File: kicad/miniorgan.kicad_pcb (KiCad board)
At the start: 2 copper layers, 202 x 125 mm, 236 parts, among them J1 Conn_01x03, J10 Conn_01x03, J11 Conn_01x03, J2 POWER_IN, J3 AudioJack3, J4 Conn_01x05, J5 Conn_01x04, J6 Conn_01x06, J7 Barrel_Jack_Switch, U1 40106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

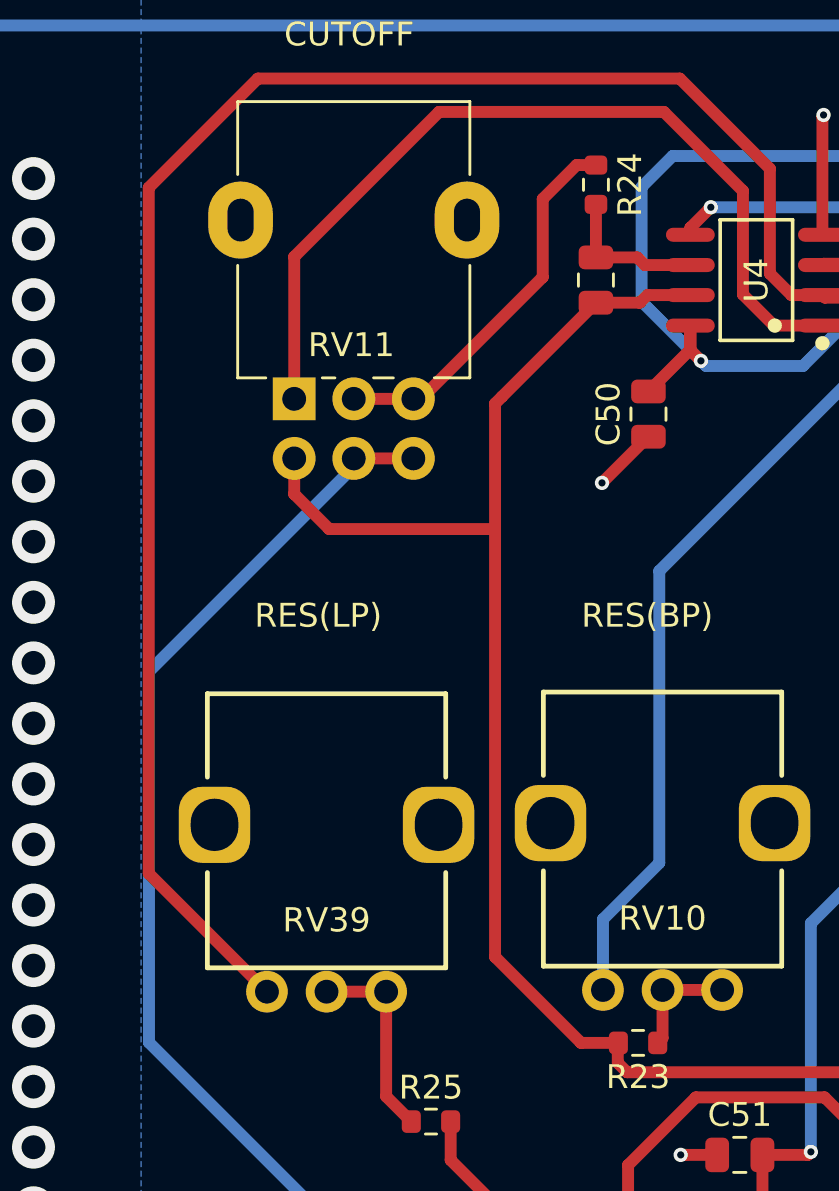
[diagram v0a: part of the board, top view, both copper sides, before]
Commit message: update footprint of dual gang potentiometer to accomodate larger poti
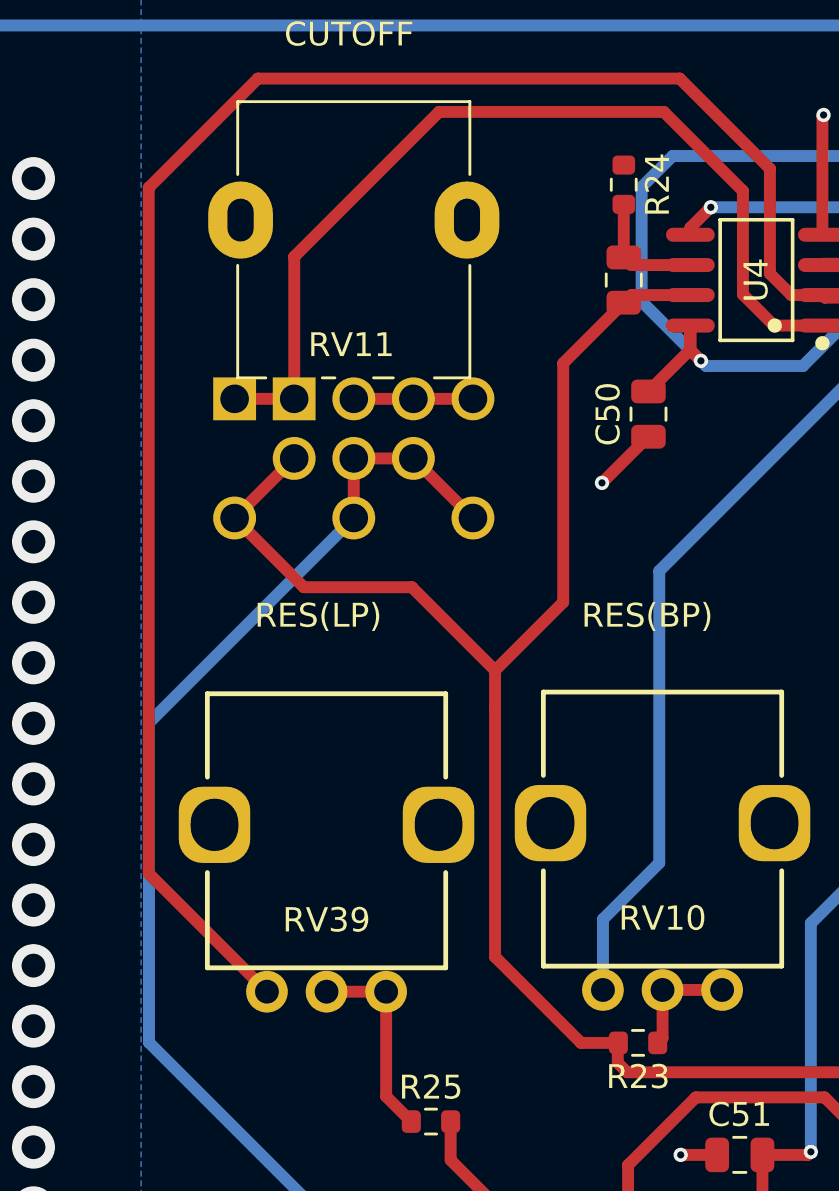
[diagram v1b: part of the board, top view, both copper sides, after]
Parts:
- moved C11 1.17 mm to (145.2, 43.1)
- moved R24 1.17 mm to (145.2, 39.1)
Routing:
- net Net-(R24-Pad1): track 16.1 -> 5.00 mm
- net /Filter/band pass: track 76.7 -> 82.6 mm
- net Net-(R26-Pad1): track 45.8 -> 49.7 mm
- net /Filter/high pass: track 68.1 -> 70.6 mm
- net Net-(U4B--): track 6.32 -> 5.15 mm
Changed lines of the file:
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@@
 	(footprint "Capacitor_SMD:C_0805_2012Metric"
 		(layer "F.Cu")
-		(at 144.0826 43.05415 -90)
+		(at 145.25 43.05415 -90)
 		(descr "Capacitor SMD 0805 (2012 Metric), square (rectangular) end terminal, IPC_7351 nominal, (Body size source: IPC-SM-782 page 76, https://www.pcb-3d.com/wordpress/wp-content/uploads/ipc-sm-782a_amendment_1_and_2.pdf, https://docs.google.com/spreadsheets/d/1BsfQQcO9C6DZCsRaXUlFlo91Tg2WpOkGARC1WS5S8t0/edit?usp=sharing), generated with kicad-footprint-generator")
 		(tags "capacitor")
@@
 	(footprint "Resistor_SMD:R_0603_1608Metric"
 		(layer "F.Cu")
-		(at 144.0826 39.05415 -90)
+		(at 145.25 39.05415 -90)
 		(descr "Resistor SMD 0603 (1608 Metric), square (rectangular) end terminal, IPC_7351 nominal, (Body size source: IPC-SM-782 page 72, https://www.pcb-3d.com/wordpress/wp-content/uploads/ipc-sm-782a_amendment_1_and_2.pdf), generated with kicad-footprint-generator")
 		(tags "resistor")
@@
 			)
 		)
+		(property "Notes" "Alternative RV16A01F-41-15R1-B1M"
+			(at 0 0 0)
+			(unlocked yes)
+			(layer "F.Fab")
+			(hide yes)
+			(effects
+				(font
+					(size 1 1)
+					(thickness 0.15)
+				)
+			)
+		)
 		(property ki_fp_filters "Potentiometer*")
 		(sheetname "Filter")
@@
 		)
 		(pad "1" thru_hole rect
+			(at 0 -2.5 180)
+			(size 1.8 1.8)
+			(drill 1.2)
+			(layers "*.Cu" "*.Mask")
+			(remove_unused_layers no)
+			(net 105 "/Filter/high pass")
+			(pinfunction "1")
+			(pintype "passive")
+		)
+		(pad "1" thru_hole rect
 			(at 0 0 180)
 			(size 1.8 1.8)
-			(drill 1)
+			(drill 1.2)
 			(layers "*.Cu" "*.Mask")
 			(remove_unused_layers no)
@@
 			(at 0 2.5 180)
 			(size 1.8 1.8)
-			(drill 1)
+			(drill 1.2)
 			(layers "*.Cu" "*.Mask")
 			(remove_unused_layers no)
@@
 			(at 0 5 180)
 			(size 1.8 1.8)
-			(drill 1)
+			(drill 1.2)
+			(layers "*.Cu" "*.Mask")
+			(remove_unused_layers no)
+			(net 106 "Net-(R24-Pad1)")
+			(pinfunction "3")
+			(pintype "passive")
+		)
+		(pad "3" thru_hole circle
+			(at 0 7.5 180)
+			(size 1.8 1.8)
+			(drill 1.2)
 			(layers "*.Cu" "*.Mask")
 			(remove_unused_layers no)
@@
 		)
 		(pad "4" thru_hole circle
+			(at -5 -2.5 180)
+			(size 1.8 1.8)
+			(drill 1.2)
+			(layers "*.Cu" "*.Mask")
+			(remove_unused_layers no)
+			(net 20 "/Filter/band pass")
+			(pinfunction "4")
+			(pintype "passive")
+		)
+		(pad "4" thru_hole circle
 			(at -2.5 0 180)
 			(size 1.8 1.8)
-			(drill 1)
+			(drill 1.2)
 			(layers "*.Cu" "*.Mask")
 			(remove_unused_layers no)
@@
 		)
 		(pad "5" thru_hole circle
+			(at -5 2.5 180)
+			(size 1.8 1.8)
+			(drill 1.2)
+			(layers "*.Cu" "*.Mask")
+			(remove_unused_layers no)
+			(net 107 "Net-(R26-Pad1)")
+			(pinfunction "5")
+			(pintype "passive")
+		)
+		(pad "5" thru_hole circle
 			(at -2.5 2.5 180)
 			(size 1.8 1.8)
-			(drill 1)
+			(drill 1.2)
 			(layers "*.Cu" "*.Mask")
 			(remove_unused_layers no)
@@
 		)
 		(pad "6" thru_hole circle
+			(at -5 7.5 180)
+			(size 1.8 1.8)
+			(drill 1.2)
+			(layers "*.Cu" "*.Mask")
+			(remove_unused_layers no)
+			(net 107 "Net-(R26-Pad1)")
+			(pinfunction "6")
+			(pintype "passive")
+		)
+		(pad "6" thru_hole circle
 			(at -2.5 5 180)
 			(size 1.8 1.8)
-			(drill 1)
+			(drill 1.2)
 			(layers "*.Cu" "*.Mask")
 			(remove_unused_layers no)
@@
 	)
 	(segment
-		(start 131.4226 52.0326)
-		(end 132.89 53.5)
+		(start 128.9226 53.03715)
+		(end 131.4226 50.53715)
 		(width 0.5)
 		(layer "F.Cu")
@@
 	)
 	(segment
-		(start 145 75.08255)
-		(end 145 75.9)
+		(start 139.85 71.44955)
+		(end 139.85 61.02)
 		(width 0.5)
 		(layer "F.Cu")
@@
 	)
 	(segment
-		(start 132.89 53.5)
-		(end 139.81 53.5)
+		(start 142.71 46.54415)
+		(end 145.25 44.00415)
+		(width 0.5)
+		(layer "F.Cu")
+		(net 20)
+	)
+	(segment
+		(start 145 75.08255)
+		(end 145 75.9)
 		(width 0.5)
 		(layer "F.Cu")
@@
 	)
 	(segment
-		(start 139.81 53.5)
-		(end 139.85 53.46)
+		(start 139.85 61.02)
+		(end 139.85 59.43)
 		(width 0.5)
 		(layer "F.Cu")
@@
 	)
 	(segment
-		(start 131.4226 50.53715)
-		(end 131.4226 52.0326)
+		(start 145.0244 75.05815)
+		(end 143.4586 75.05815)
 		(width 0.5)
 		(layer "F.Cu")
@@
 	)
 	(segment
-		(start 140.1456 47.94115)
-		(end 144.0826 44.00415)
+		(start 142.71 56.57)
+		(end 142.71 46.54415)
 		(width 0.5)
 		(layer "F.Cu")
@@
 	)
 	(segment
-		(start 139.85 71.44955)
-		(end 139.85 48.23675)
+		(start 145 75.9)
+		(end 145.39 76.29)
 		(width 0.5)
 		(layer "F.Cu")
@@
 	)
 	(segment
-		(start 145.92585 44.00415)
-		(end 146.24585 43.68415)
+		(start 148.0436 43.68415)
+		(end 145.57 43.68415)
 		(width 0.5)
 		(layer "F.Cu")
@@
 	)
 	(segment
-		(start 145 75.9)
-		(end 145.39 76.29)
+		(start 145.57 43.68415)
+		(end 145.25 44.00415)
 		(width 0.5)
 		(layer "F.Cu")
@@
 	)
 	(segment
-		(start 145.0244 75.05815)
-		(end 143.4586 75.05815)
+		(start 139.85 59.43)
+		(end 136.36 55.94)
 		(width 0.5)
 		(layer "F.Cu")
@@
 	)
 	(segment
-		(start 146.24585 43.68415)
-		(end 148.0436 43.68415)
+		(start 131.82545 55.94)
+		(end 128.9226 53.03715)
 		(width 0.5)
 		(layer "F.Cu")
@@
 	)
 	(segment
-		(start 139.85 48.23675)
-		(end 140.1456 47.94115)
+		(start 139.85 59.43)
+		(end 142.71 56.57)
 		(width 0.5)
 		(layer "F.Cu")
@@
 	)
 	(segment
-		(start 144.0826 44.00415)
-		(end 145.92585 44.00415)
+		(start 145.0244 75.05815)
+		(end 145 75.08255)
 		(width 0.5)
 		(layer "F.Cu")
@@
 	)
 	(segment
-		(start 145.0244 75.05815)
-		(end 145 75.08255)
+		(start 136.36 55.94)
+		(end 131.82545 55.94)
 		(width 0.5)
 		(layer "F.Cu")
@@
 	)
 	(segment
-		(start 144.0826 39.87915)
-		(end 144.0826 42.10415)
-		(width 0.5)
-		(layer "F.Cu")
-		(net 23)
-	)
-	(segment
-		(start 145.81415 42.10415)
-		(end 146.13415 42.42415)
+		(start 148.0436 42.42415)
+		(end 145.57 42.42415)
 		(width 0.5)
 		(layer "F.Cu")
@@
 	)
 	(segment
-		(start 144.0826 42.10415)
-		(end 145.81415 42.10415)
+		(start 145.57 42.42415)
+		(end 145.25 42.10415)
 		(width 0.5)
 		(layer "F.Cu")
@@
 	)
 	(segment
-		(start 146.13415 42.42415)
-		(end 148.0436 42.42415)
+		(start 145.25 39.87915)
+		(end 145.25 42.10415)
 		(width 0.5)
 		(layer "F.Cu")
@@
 	)
 	(segment
+		(start 128.9226 48.03715)
+		(end 131.4226 48.03715)
+		(width 0.5)
+		(layer "F.Cu")
+		(net 105)
+	)
+	(segment
 		(start 131.4226 48.03715)
 		(end 131.4226 42.0774)
@@
 	)
 	(segment
-		(start 136.74285 48.03715)
+		(start 133.9226 48.03715)
 		(end 136.4226 48.03715)
 		(width 0.5)
@@
 	)
 	(segment
-		(start 141.85 42.93)
-		(end 136.74285 48.03715)
-		(width 0.5)
-		(layer "F.Cu")
-		(net 106)
-	)
-	(segment
-		(start 141.85 39.65)
-		(end 141.85 42.93)
-		(width 0.5)
-		(layer "F.Cu")
-		(net 106)
-	)
-	(segment
-		(start 133.9226 48.03715)
-		(end 136.4226 48.03715)
+		(start 136.4226 48.03715)
+		(end 138.9226 48.03715)
 		(width 0.5)
 		(layer "F.Cu")
@@
 	)
 	(segment
-		(start 144.0826 38.22915)
-		(end 143.27085 38.22915)
+		(start 133.9226 50.53715)
+		(end 136.4226 50.53715)
 		(width 0.5)
 		(layer "F.Cu")
-		(net 106)
+		(net 107)
 	)
 	(segment
-		(start 143.27085 38.22915)
-		(end 141.85 39.65)
+		(start 136.5896 84.71015)
+		(end 135.00015 84.71015)
 		(width 0.5)
 		(layer "F.Cu")
-		(net 106)
+		(net 107)
 	)
 	(segment
 		(start 133.9226 50.53715)
-		(end 136.4226 50.53715)
+		(end 133.9226 53.03715)
 		(width 0.5)
 		(layer "F.Cu")
@@
 	)
 	(segment
-		(start 136.5896 84.71015)
-		(end 135.00015 84.71015)
+		(start 135.00015 84.71015)
+		(end 133.39 83.1)
 		(width 0.5)
 		(layer "F.Cu")
@@
 	)
 	(segment
-		(start 135.00015 84.71015)
-		(end 133.39 83.1)
+		(start 136.4226 50.53715)
+		(end 138.9226 53.03715)
 		(width 0.5)
 		(layer "F.Cu")
@@
 	)
 	(segment
-		(start 133.39 83.1)
-		(end 125.33 75.04)
+		(start 125.33 75.04)
+		(end 125.33 61.62975)
 		(width 0.5)
 		(layer "B.Cu")
@@
 	)
 	(segment
-		(start 125.33 59.48)
-		(end 133.9226 50.8874)
+		(start 133.39 83.1)
+		(end 125.33 75.04)
 		(width 0.5)
 		(layer "B.Cu")
@@
 	)
 	(segment
-		(start 133.9226 50.8874)
-		(end 133.9226 50.53715)
+		(start 125.33 61.62975)
+		(end 133.9226 53.03715)
 		(width 0.5)
 		(layer "B.Cu")
@@
 	)
 	(segment
-		(start 125.33 75.04)
-		(end 125.33 59.48)
+		(start 133.9226 50.8874)
+		(end 133.9226 50.53715)
 		(width 0.5)
 		(layer "B.Cu")

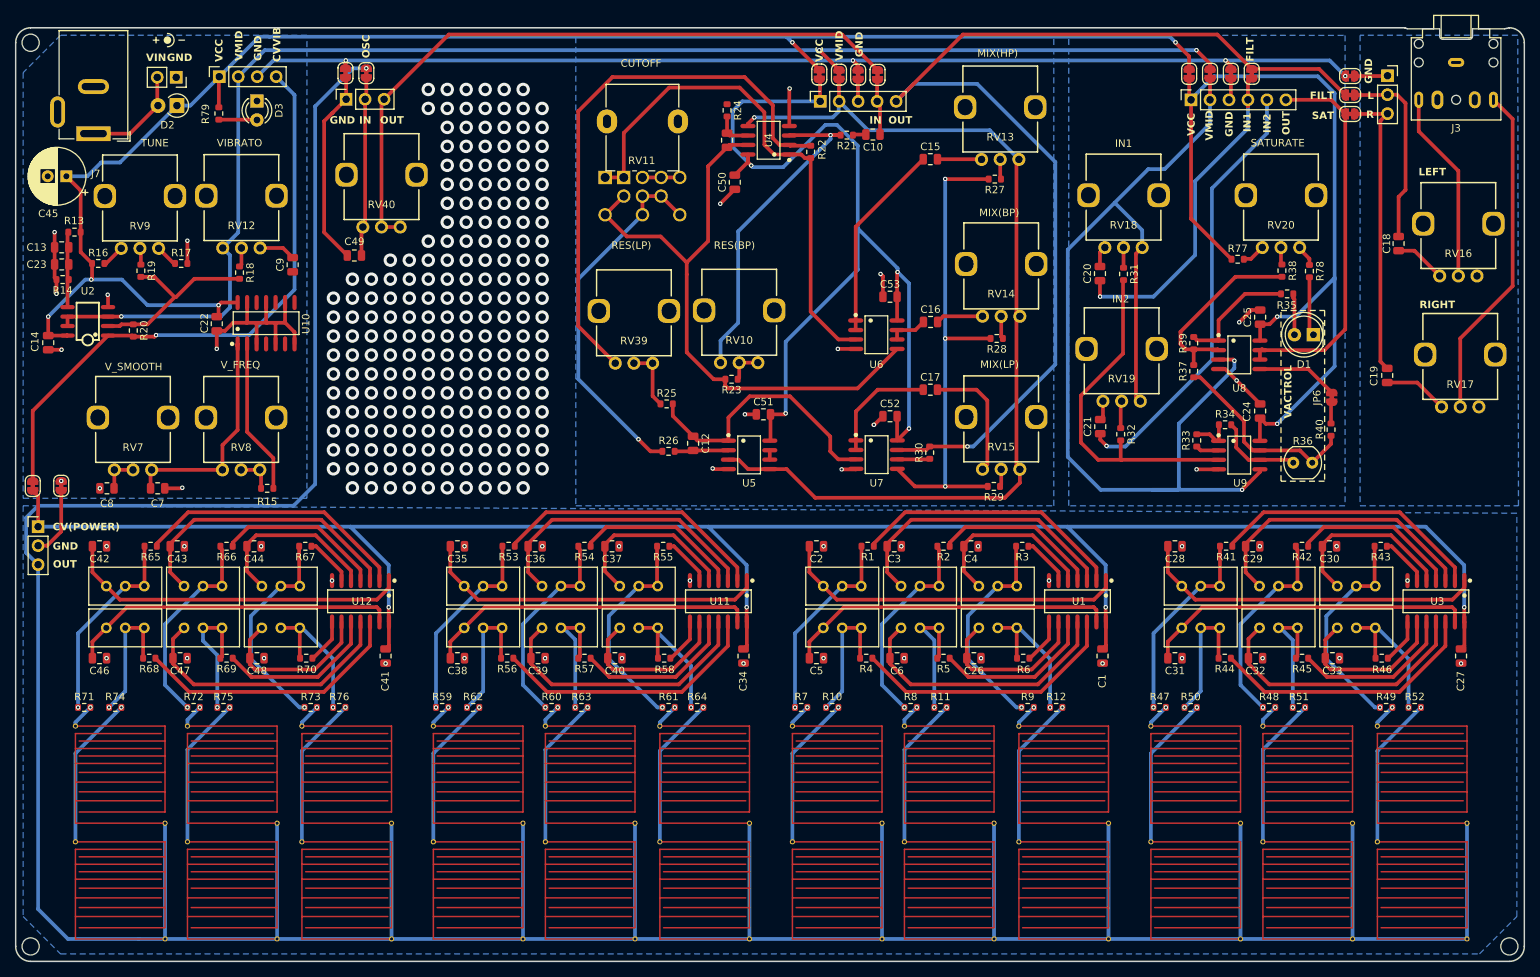
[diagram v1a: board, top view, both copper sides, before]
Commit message: fix mixers in filter and compressor, update pcb
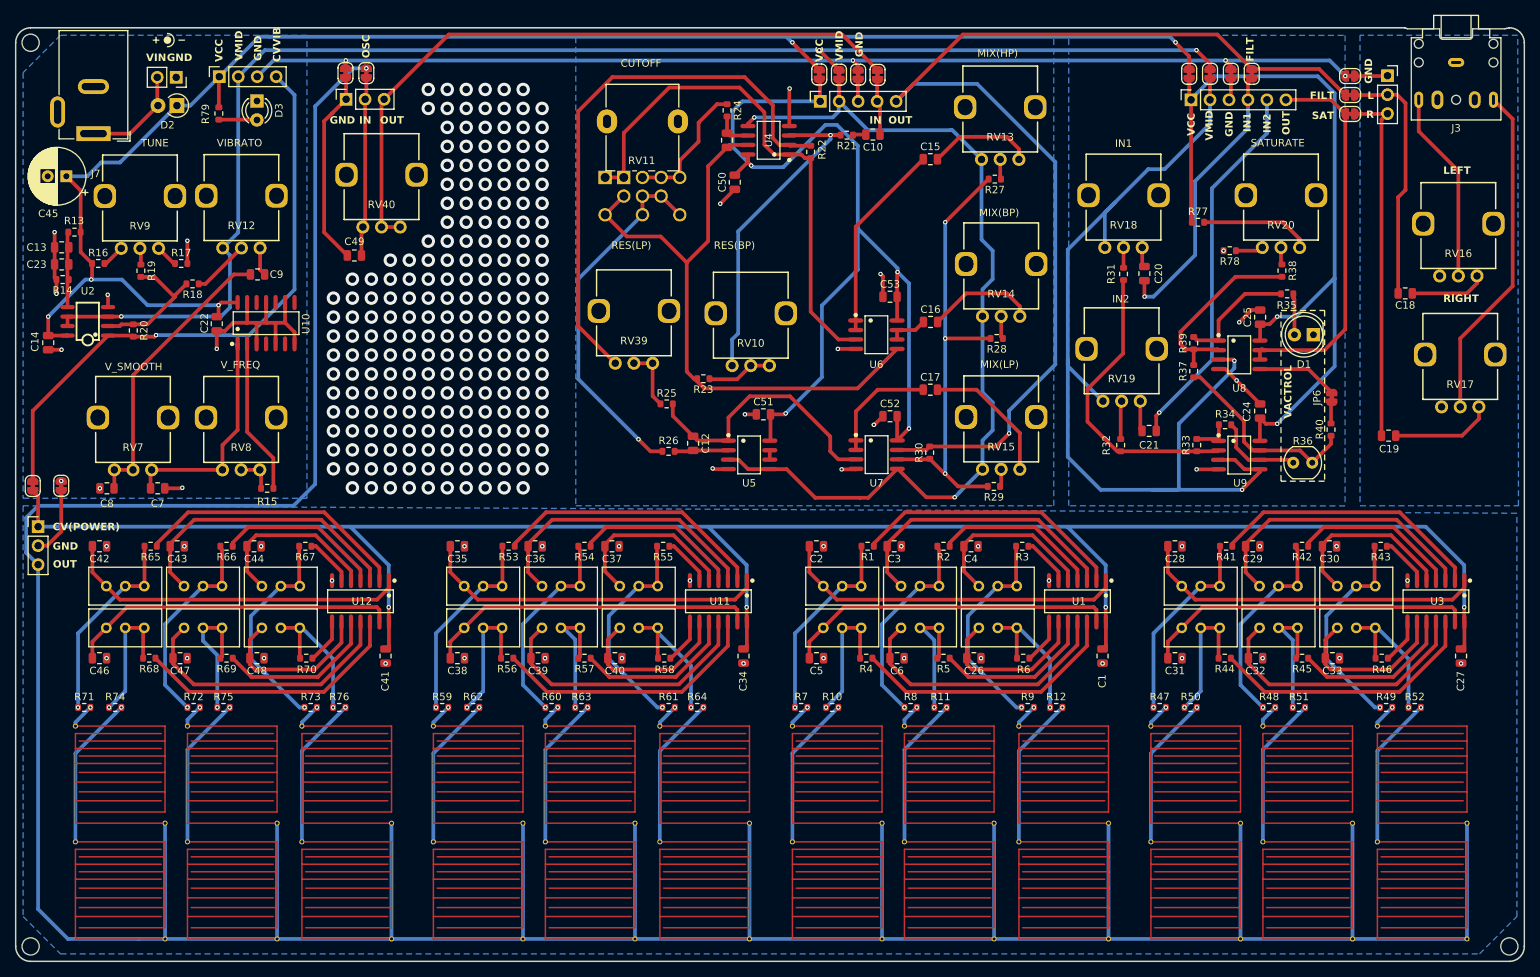
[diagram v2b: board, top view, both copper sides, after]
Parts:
- RV13, RV14, RV15: value 50K -> A100K
- RV16, RV17: value 100K -> A100K
- moved R78 11.0 mm to (212.6, 57.8), turned to 180 degrees
- moved C19 8.06 mm to (233.8, 82.6), turned to 0 degrees
- moved R77 7.27 mm to (208.3, 54.0)
- moved C18 6.72 mm to (236.1, 63.6), turned to 0 degrees
- moved C21 6.57 mm to (201.8, 82.0), turned to 180 degrees
- moved R18 6.46 mm to (73.7, 62.3), turned to 180 degrees
- moved C20 5.95 mm to (201.1, 60.9)
- moved C9 4.87 mm to (82.4, 61.0), turned to 0 degrees
- moved R23 3.78 mm to (142.1, 75.0)
- moved RV10 1.60 mm to (148.4, 66.2)
- moved R32 1.46 mm to (198.0, 83.9)
- moved R33 0.63 mm to (208.1, 83.9)
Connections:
- R27 pad 2: Net-(U7B-+) -> Net-(U7B--)
- R28 pad 2: Net-(U7B-+) -> Net-(U7B--)
- R29 pad 2: Net-(U7B-+) -> Net-(U7B--)
- R31 pad 2: Net-(U9A-+) -> Net-(U9A--)
- R32 pad 2: Net-(U9A-+) -> Net-(U9A--)
- RV13 pad 1: Net-(C15-Pad2) -> /Filter/VMID
- RV13 pad 3: /Filter/VMID -> Net-(C15-Pad2)
- RV14 pad 1: Net-(C16-Pad2) -> /Filter/VMID
- RV14 pad 3: /Filter/VMID -> Net-(C16-Pad2)
- RV15 pad 1: Net-(C17-Pad2) -> /Filter/VMID
- RV15 pad 3: /Filter/VMID -> Net-(C17-Pad2)
- RV16 pad 1: Net-(C18-Pad2) -> /output/GND
- RV16 pad 3: /output/GND -> Net-(C18-Pad2)
- RV17 pad 1: Net-(C19-Pad2) -> /output/GND
- RV17 pad 3: /output/GND -> Net-(C19-Pad2)
- RV18 pad 1: Net-(C20-Pad2) -> /vactrol compressor/VMID
- RV18 pad 3: /vactrol compressor/VMID -> Net-(C20-Pad2)
- RV19 pad 1: Net-(C21-Pad2) -> /vactrol compressor/VMID
- RV19 pad 3: /vactrol compressor/VMID -> Net-(C21-Pad2)
- RV20 pad 1: Net-(R77-Pad2) -> Net-(R78-Pad1)
- RV20 pad 3: Net-(R78-Pad1) -> Net-(R77-Pad2)
- U7 pad 5: Net-(U7B-+) -> /Filter/VMID
- U9 pad 3: Net-(U9A-+) -> /vactrol compressor/VMID
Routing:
- net Net-(U7B-+): track 66.2 -> 0.00 mm, vias 3 -> 0
- net Net-(U7B--): track 4.37 -> 61.6 mm, vias 0 -> 3
- net Net-(U9A-+): track 46.1 -> 0.00 mm
- net Net-(U9A--): track 3.13 -> 40.2 mm
- net /power/VLFO: track 5.28 -> 39.3 mm
- net Net-(R24-Pad1): track 5.00 -> 18.2 mm
- net Net-(R77-Pad2): track 3.12 -> 15.1 mm
- net /output/IN_R: track 39.3 -> 47.8 mm
- net /vactrol compressor/IN2: track 58.8 -> 50.5 mm
- net Net-(C16-Pad2): track 6.32 -> 14.6 mm
- net Net-(C15-Pad2): track 5.92 -> 14.2 mm
- net /vactrol compressor/VMID: track 143.9 -> 135.9 mm
- net /vactrol compressor/VCC: track 115.9 -> 108.2 mm
- net /output/IN_L: track 25.5 -> 33.1 mm
- net Net-(U2A--): track 25.9 -> 18.6 mm
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
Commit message: add local changes
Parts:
- moved C19 23.4 mm to (233.7, 59.2), turned to -90 degrees
- moved C18 17.8 mm to (236.1, 45.8), turned to -90 degrees
- moved R77 8.72 mm to (211.1, 45.8)
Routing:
- net /output/IN_R: track 47.8 -> 23.6 mm
- net /output/IN_L: track 33.1 -> 14.0 mm
- net Net-(C19-Pad2): track 13.7 -> 23.7 mm
- net Net-(C18-Pad2): track 10.2 -> 18.5 mm
- net /vactrol compressor/VCC: track 108.2 -> 101.8 mm
- net Net-(R77-Pad2): track 15.1 -> 17.8 mm
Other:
- board text added: "organ 1_20250204"
- board text removed: "organ 20250203"
